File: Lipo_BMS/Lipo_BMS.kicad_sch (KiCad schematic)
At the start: 59 parts, among them J1 Deans connector male, J101 XT30, J102 B4B-XH-A(LF)(SN), J103 B4B-XH-A(LF)(SN), J2 XT30, J3 STL1550/2G-3.5, J4 54-00286, J5 Terminal block, J6 B3B-PH-SM4-TB(LF)(SN), Q101 SI4459ADY-T1-GE3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

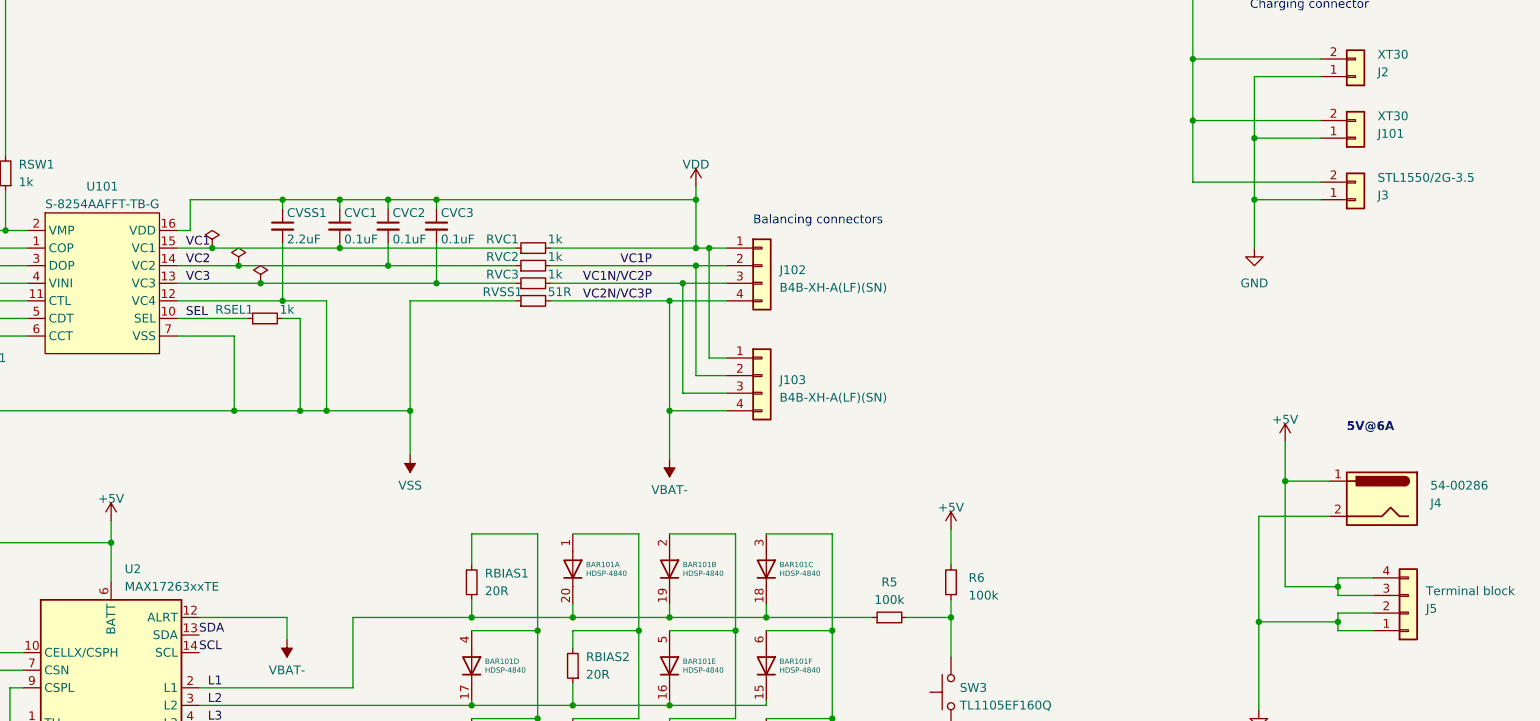
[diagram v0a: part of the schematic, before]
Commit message: Added BOM to LiPo board
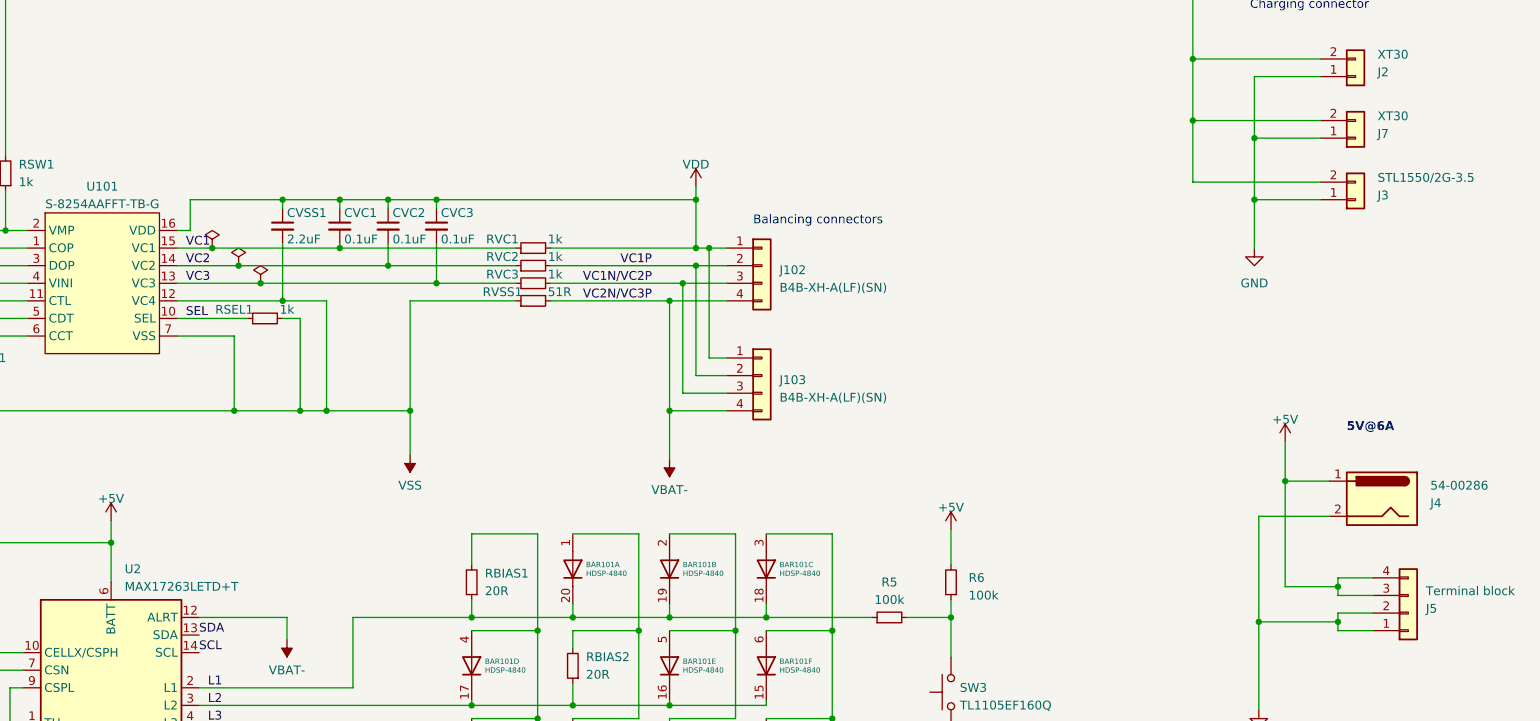
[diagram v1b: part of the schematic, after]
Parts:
- CCCT1, CCDT1, CVC1, CVC2, CVC3: Distributor (none) -> Digikey; Distributor ref (none) -> 478-5778-1-ND; Manufacturer ref (none) -> 06035C104JAT2A
- CVSS1: Distributor (none) -> Digikey; Distributor ref (none) -> 490-GRM188Z71C225ME43JCT-ND; Manufacturer ref (none) -> GRM188Z71C225ME43J
- F101: Distributor (none) -> Digikey; Distributor ref (none) -> 36-3587-20CT-ND; Manufacturer ref (none) -> 3587-20TR
- H101, H102, H103, H104: Distributor (none) -> Digikey; Distributor ref (none) -> RPC3611-ND; Manufacturer ref (none) -> CBTS005A
- J1: Distributor (none) -> Digikey; Distributor ref (none) -> 1568-1659-ND; Manufacturer ref (none) -> PRT-11864
- J102, J103: Distributor (none) -> Digikey; Distributor ref (none) -> 455-2249-ND; Manufacturer ref (none) -> B4B-XH-A(LF)(SN)
- J2: Distributor (none) -> Digikey; Distributor ref (none) -> 1738-1436-ND; Manufacturer ref (none) -> FIT0586
- J3: Distributor (none) -> Distrelec; Distributor ref (none) -> 148-41-220; Manufacturer ref (none) -> STL1550/2G-3.5-V-GREEN
- J7: renamed from J101; Distributor (none) -> Digikey; Distributor ref (none) -> 1738-1436-ND; Manufacturer ref (none) -> FIT0586
- R4: Distributor (none) -> Digikey; Distributor ref (none) -> 541-MCT0603MD1304BP500CT-ND; Manufacturer ref (none) -> MCT0603MD1304BP500
- R5, R6: Distributor (none) -> Digikey; Distributor ref (none) -> 311-100KHRCT-ND; Manufacturer ref (none) -> RC0603FR-07100KL
- R7: Distributor (none) -> Digikey; Distributor ref (none) -> YAG1578CT-ND; Manufacturer ref (none) -> RT0603BRD07200KL
- RBIAS1, RBIAS2, RBIAS3, RBIAS4: Distributor (none) -> Digikey; Distributor ref (none) -> P20.00BYCT-ND; Manufacturer ref (none) -> ERJ-PA3F20R0V
- RCOP1: Distributor (none) -> Digikey; Distributor ref (none) -> 1292-WR06X1004FTLCT-ND; Manufacturer ref (none) -> WR06X1004FTL
- RCTL1, RSEL1, RSW1, RVC1, RVC2, RVC3, RVINI1: Distributor (none) -> Digikey; Distributor ref (none) -> RNCP0603FTD1K00CT-ND; Manufacturer ref (none) -> RNCP0603FTD1K00
- RDOP1, RVMP1: Distributor (none) -> Digikey; Distributor ref (none) -> 13-RC0603FR-135K1LCT-ND; Manufacturer ref (none) -> RC0603FR-135K1L
- RSENSE1: Distributor (none) -> Digikey; Distributor ref (none) -> 2037-VSRP1206S1-R010FCT-ND; Manufacturer ref (none) -> VSRP1206S1-R010F
- RVSS1: Distributor (none) -> Digikey; Distributor ref (none) -> 311-51.0HRCT-ND; Manufacturer ref (none) -> RC0603FR-0751RL
- SW1: Distributor (none) -> Digikey; Distributor ref (none) -> 450301014042-ND; Manufacturer ref (none) -> 450301014042
- SW2: Distributor (none) -> Digikey; Distributor ref (none) -> EG1832-ND; Manufacturer ref (none) -> TL1105EF250Q7.3RED
- SW3: Distributor (none) -> Digikey; Distributor ref (none) -> EG1831-ND; Manufacturer ref (none) -> TL1105EF160Q
- U1: Distributor (none) -> Digikey; Distributor ref (none) -> 454-1280-ND; Manufacturer ref (none) -> LDO06C-005W05-HJ
- U101: Distributor (none) -> Mouser; Distributor ref (none) -> 628-S-8254AAFFT-TB-G; Manufacturer ref (none) -> S-8254AAFFT-TB-G
- U2: value MAX17263xxTE -> MAX17263LETD+T; Distributor (none) -> Digikey; Distributor ref (none) -> 175-MAX17263LETD+TCT-ND; Manufacturer ref (none) -> MAX17263LETD+T
